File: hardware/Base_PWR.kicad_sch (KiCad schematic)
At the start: 1 part

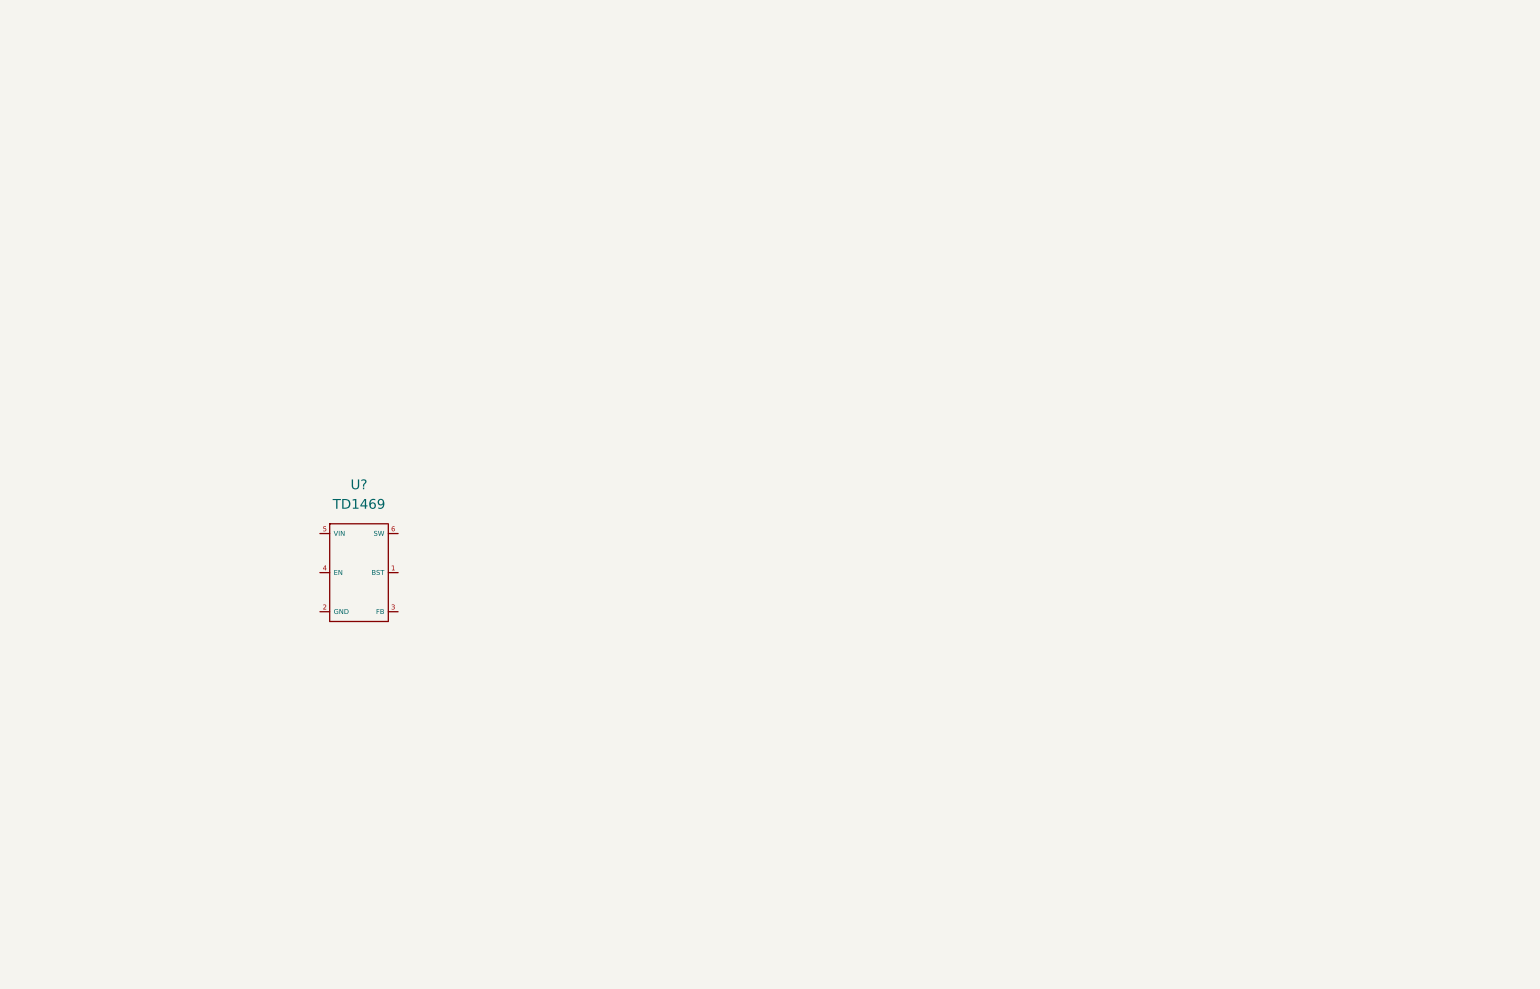
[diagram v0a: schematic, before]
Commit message: Update MCU and Base_PWR.
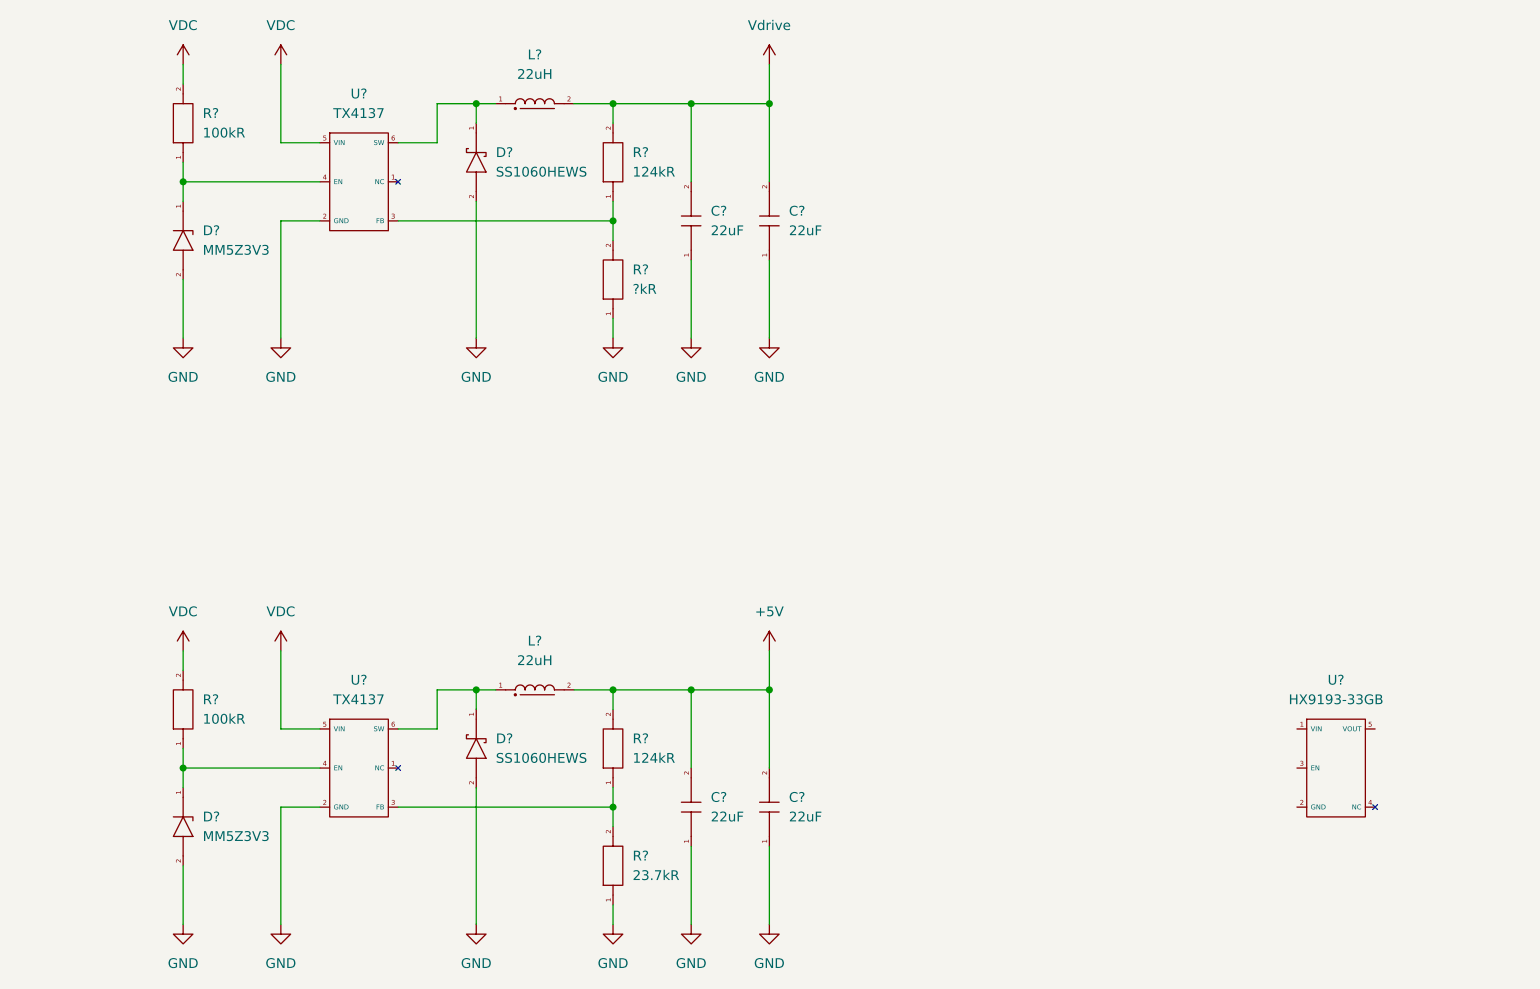
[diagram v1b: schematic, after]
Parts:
- removed U?: TD1469, GENERAL_SMALL-SEMI_SMD:SOT-23-6, symbol Power_DC-DC_convertor:TD1469
- added C? (x4): 22uF, GENERAL_RCL_SMD:C0805(2012M), symbol Basic_passive_components:Capacitor
- added D? (x2): MM5Z3V3, GENERAL_2-PIN_PLASTIC_SMD:SOD-523, symbol Basic_semiconductor:Diode_Zener
- added D? (x2): SS1060HEWS, POWER_DIODE_SMD:SOD-323HE, symbol Basic_semiconductor:Diode_Schottky
- added L? (x2): 22uH, symbol Basic_passive_components:Power_Inductor
- added R?: ?kR, GENERAL_RCL_SMD:C0402(1005M), symbol Basic_passive_components:Resistor
- added R? (x2): 100kR, GENERAL_RCL_SMD:C0402(1005M), symbol Basic_passive_components:Resistor
- added R? (x2): 124kR, GENERAL_RCL_SMD:C0402(1005M), symbol Basic_passive_components:Resistor
- added R?: 23.7kR, GENERAL_RCL_SMD:C0402(1005M), symbol Basic_passive_components:Resistor
- added U? (x2): TX4137, GENERAL_SMALL-SEMI_SMD:SOT-23-6, symbol Power_DC-DC_convertor:TX4137
- added U?: HX9193-33GB, GENERAL_SMALL-SEMI_SMD:SOT-23-5, symbol Power_LDO:HX9193-33GB
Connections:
- new net: D?.1 (Cathode), L?.1, U?.6 (SW) (x2)
- new net: R?.1, R?.2, U?.3 (FB) (x2)
- new net: D?.1 (Cathode), R?.1, U?.4 (EN) (x2)
- new net +5V: C?.2, C?.2, L?.2, R?.2
- new net GND: C?.1, C?.1, C?.1, C?.1, D?.2 (Anode), D?.2 (Anode), D?.2 (Anode), D?.2 (Anode), R?.1, R?.1, U?.2 (GND), U?.2 (GND)
- new net VDC: R?.2, R?.2, U?.5 (VIN), U?.5 (VIN)
- new net Vdrive: C?.2, C?.2, L?.2, R?.2

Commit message: Nightly update
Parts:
- removed D?: MM5Z3V3, GENERAL_2-PIN_PLASTIC_SMD:SOD-523, symbol Basic_semiconductor:Diode_Zener
- added C? (x2): 100nF, GENERAL_RCL_SMD:C0603(1608M), symbol Basic_passive_components:Capacitor
- added D?: MM3Z3V3W, GENERAL_2-PIN_PLASTIC_SMD:SOD-323, symbol Basic_semiconductor:Diode_Zener
- added R?: 10kR, GENERAL_RCL_SMD:C0603(1608M), symbol Basic_passive_components:Resistor
- D?: value MM5Z3V3 -> MM3Z3V3W; footprint GENERAL_2-PIN_PLASTIC_SMD:SOD-523 -> GENERAL_2-PIN_PLASTIC_SMD:SOD-323
- R? (x6): footprint GENERAL_RCL_SMD:C0402(1005M) -> GENERAL_RCL_SMD:C0603(1608M)
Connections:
- net +5V: now also U?.1 (VIN), C?.2, R?.2
- net GND: now also U?.2 (GND), C?.1, C?.1, D?.2 (Anode)
- net at R?.1, U?.4 (EN): now also D?.1 (Cathode)
- net at U?.3 (EN): now also R?.1
- net +3V3: now reaches U?.5 (VOUT)
- net +3V3: now also C?.2
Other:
- moved on the sheet: D?, R?

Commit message: Nightly update
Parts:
- removed C? (x4): 22uF, GENERAL_RCL_SMD:C0805(2012M), symbol Basic_passive_components:Capacitor
- removed D?: MM3Z3V3W, GENERAL_2-PIN_PLASTIC_SMD:SOD-323, symbol Basic_semiconductor:Diode_Zener
- removed D?: SS1060HEWS, POWER_DIODE_SMD:SOD-323HE, symbol Basic_semiconductor:Diode_Schottky
- removed R?: 124kR, GENERAL_RCL_SMD:C0603(1608M), symbol Basic_passive_components:Resistor
- removed R?: 100kR, GENERAL_RCL_SMD:C0603(1608M), symbol Basic_passive_components:Resistor
- added C? (x4): 22uF, 001_GN_RCL_SMD:C0805(2012M), symbol 001_Basic_PassiveComponents:101_Capacitor
- added C? (x4): 10uF, 001_GN_RCL_SMD:C1206(3216M), symbol 001_Basic_PassiveComponents:101_Capacitor
- added D?: MM3Z3V3W, 002_GN_TWO-PIN_PLASTIC_SMD:SOD-323, symbol Basic_semiconductor:Diode_Zener
- added D?: SS1060HEWS, 002_GN_TWO-PIN_PLASTIC_SMD:SOD-323HE, symbol 002_Basic_SingleSemiconductor:002_Diode_Schottky
- added R?: 124kR, 001_GN_RCL_SMD:R0402(1005M), symbol 001_Basic_PassiveComponents:001_Resistor
- added R?: 100kR, 001_GN_RCL_SMD:R0402(1005M), symbol 001_Basic_PassiveComponents:001_Resistor
- C? (x2): footprint GENERAL_RCL_SMD:C0603(1608M) -> 001_GN_RCL_SMD:C0402(1005M); symbol Basic_passive_components:Capacitor -> 001_Basic_PassiveComponents:101_Capacitor; Symbol type (none) -> Alternate Source
- D?: footprint GENERAL_2-PIN_PLASTIC_SMD:SOD-323 -> 002_GN_TWO-PIN_PLASTIC_SMD:SOD-323
- D?: footprint POWER_DIODE_SMD:SOD-323HE -> 002_GN_TWO-PIN_PLASTIC_SMD:SOD-323HE; symbol Basic_semiconductor:Diode_Schottky -> 002_Basic_SingleSemiconductor:002_Diode_Schottky; Symbol type (none) -> Alternate Source
- R? (x5): footprint GENERAL_RCL_SMD:C0603(1608M) -> 001_GN_RCL_SMD:R0402(1005M); symbol Basic_passive_components:Resistor -> 001_Basic_PassiveComponents:001_Resistor; Symbol type (none) -> Alternate Source
- U? (x2): footprint GENERAL_SMALL-SEMI_SMD:SOT-23-6 -> 003_GN_SMALL-SEMI_SMD:SOT-23-6; symbol Power_DC-DC_convertor:TX4137 -> 204_Power_SMPS-Convertor:TX4137; Symbol type (none) -> Specified Device
- U?: footprint GENERAL_SMALL-SEMI_SMD:SOT-23-5 -> 003_GN_SMALL-SEMI_SMD:SOT-23-5; symbol Power_LDO:HX9193-33GB -> 203_Power_LDO:HX9193-33GB-N; Symbol type (none) -> Specified Device
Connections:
- net +5V: now also C?.2, C?.2, R?.2
- net GND: now also C?.1, C?.1, C?.1, C?.1, C?.1, C?.1, C?.1, C?.1, D?.2 (Anode), D?.2 (Anode)
- net VDC: now also C?.2, C?.2, C?.2, C?.2, R?.2
- net Vdrive: now also C?.2, C?.2
- net at R?.1, U?.4 (EN): now also D?.1 (Cathode)
- net at L?.1, U?.6 (SW): now also D?.1 (Cathode)
- net at R?.2, U?.3 (FB): now also R?.1
- net at D?.1 (Cathode), U?.4 (EN): now also R?.1

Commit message: Update Base_PWR
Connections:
- net PW_DRV_EN: now reaches D?.1 (Cathode), R?.1, U?.4 (EN)
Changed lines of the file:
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@@
+    (stroke (width 0) (type default) (color 0 0 0 0))
+  )
+  (wire (pts (xy 45.72 50.8) (xy 50.8 50.8))
     (stroke (width 0) (type default) (color 0 0 0 0))
   )
@@
     (stroke (width 0) (type default) (color 0 0 0 0))
   )
+  (hierarchical_label "PW_DRV_EN" (shape input) (at 45.72 50.8 180)
+    (effects (font (size 1.27 1.27)) (justify right))
+  )
   (symbol (lib_id "power:GND") (at 195.58 147.32 0) (unit 1)

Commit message: Nightly Update
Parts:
- removed D?: MM3Z3V3W, 002_GN_TWO-PIN_PLASTIC_SMD:SOD-323, symbol Basic_semiconductor:Diode_Zener
- added R?: 22kR, 001_GN_RCL_SMD:R0402(1005M), symbol 001_Basic_PassiveComponents:001_Resistor
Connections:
- net +3V3: now also C?.1, R?.1; no longer C?.2
- net +5V: now also C?.1, C?.1, C?.1, R?.1, R?.1; no longer C?.2, C?.2, C?.2, R?.2, R?.2
- net GND: now also C?.2, C?.2, C?.2, C?.2, C?.2, C?.2, C?.2, C?.2, C?.2, C?.2, R?.2, R?.2, R?.2; no longer C?.1, C?.1, C?.1, C?.1, C?.1, C?.1, C?.1, C?.1, C?.1, C?.1, R?.1, R?.1
- net PW_DRV_EN: now also R?.2; no longer R?.1
- net VDC: now also C?.1, C?.1, C?.1, C?.1, R?.1; no longer C?.2, C?.2, C?.2, C?.2, R?.2, R?.2
- net Vdrive: now also C?.1, C?.1, R?.1; no longer C?.2, C?.2, R?.2
- net at D?.1 (Cathode), U?.4 (EN): now also R?.2, R?.1; no longer R?.1
- net at U?.3 (EN): now also R?.2; no longer R?.1
- new net: R?.1, R?.2, U?.3 (FB) (x2)
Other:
- moved on the sheet: C?, R?

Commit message: Update schematics
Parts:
- R? (x2): value 124kR -> 120kR
- R?: value ?kR -> 22kR
- R?: value 23.7kR -> 22kR
- U?: value HX9193-33GB -> ME6217C33M5G; symbol 203_Power_LDO:HX9193-33GB-N -> 203_Power_LDO:ME6217C33M5G
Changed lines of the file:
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@@
       (effects (font (size 1.27 1.27)) (justify left))
     )
-    (property "Value" "124kR" (id 1) (at 111.76 125.7299 90)
+    (property "Value" "120kR" (id 1) (at 111.76 125.7299 90)
       (effects (font (size 1.27 1.27)) (justify left))
     )
@@
       (effects (font (size 1.27 1.27)) (justify left))
     )
-    (property "Value" "?kR" (id 1) (at 111.76 64.7699 90)
+    (property "Value" "22kR" (id 1) (at 111.76 64.7699 90)
       (effects (font (size 1.27 1.27)) (justify left))
     )
@@
       (effects (font (size 1.27 1.27)) (justify left))
     )
-    (property "Value" "124kR" (id 1) (at 111.76 49.5299 90)
+    (property "Value" "120kR" (id 1) (at 111.76 49.5299 90)
       (effects (font (size 1.27 1.27)) (justify left))
     )
@@
       (effects (font (size 1.27 1.27)) (justify left))
     )
-    (property "Value" "23.7kR" (id 1) (at 111.76 140.9699 90)
+    (property "Value" "22kR" (id 1) (at 111.76 140.9699 90)
       (effects (font (size 1.27 1.27)) (justify left))
     )
@@
     (pin "2")
   )
-  (symbol (lib_id "203_Power_LDO:HX9193-33GB-N") (at 203.2 127 0) (unit 1)
+  (symbol (lib_id "203_Power_LDO:ME6217C33M5G") (at 203.2 127 0) (unit 1)
     (in_bom yes) (on_board yes) (fields_autoplaced)
     (property "Reference" "U?" (id 0) (at 203.2 115.57 0))
-    (property "Value" "HX9193-33GB" (id 1) (at 203.2 118.11 0))
+    (property "Value" "ME6217C33M5G" (id 1) (at 203.2 118.11 0))
     (property "Footprint" "003_GN_SMALL-SEMI_SMD:SOT-23-5" (id 2) (at 203.2 116.84 0)
       (effects (font (size 1.27 1.27)) hide)

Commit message: Complete schematics
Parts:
- L2, L3: renamed from L?; footprint (none) -> 008_GN_POWER-CHOKE_SMD:MC-0530
- gave numbers to parts that had none: 24
